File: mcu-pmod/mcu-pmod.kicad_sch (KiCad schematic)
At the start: 51 parts, among them J1 PMOD_DEVICE, J2 XILINX_JTAG, J3 CONN_01X03, J4 CONN_01X03, J5 PMOD_HOST, U1 STM32H735-UFBGA176-25, U2 AT24MAC402

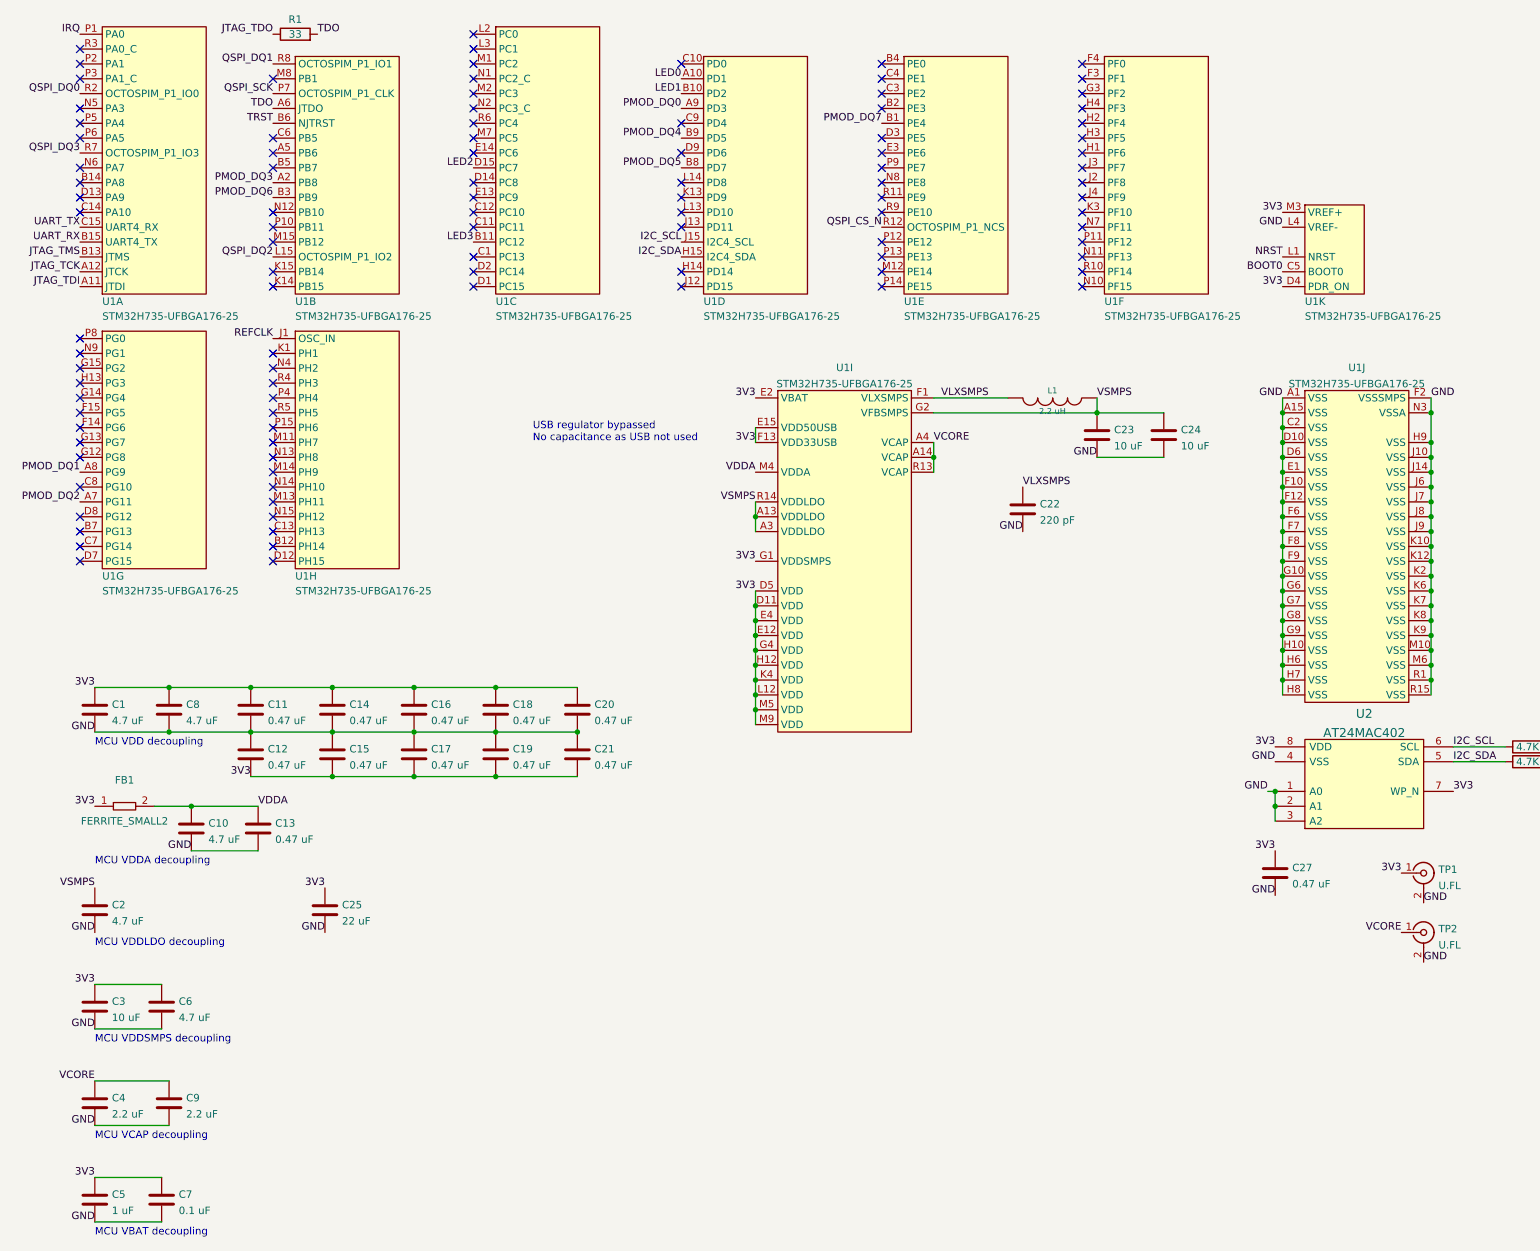
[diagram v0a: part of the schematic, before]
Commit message: v0.2 of mcu-pmod with correct STM32 footprint
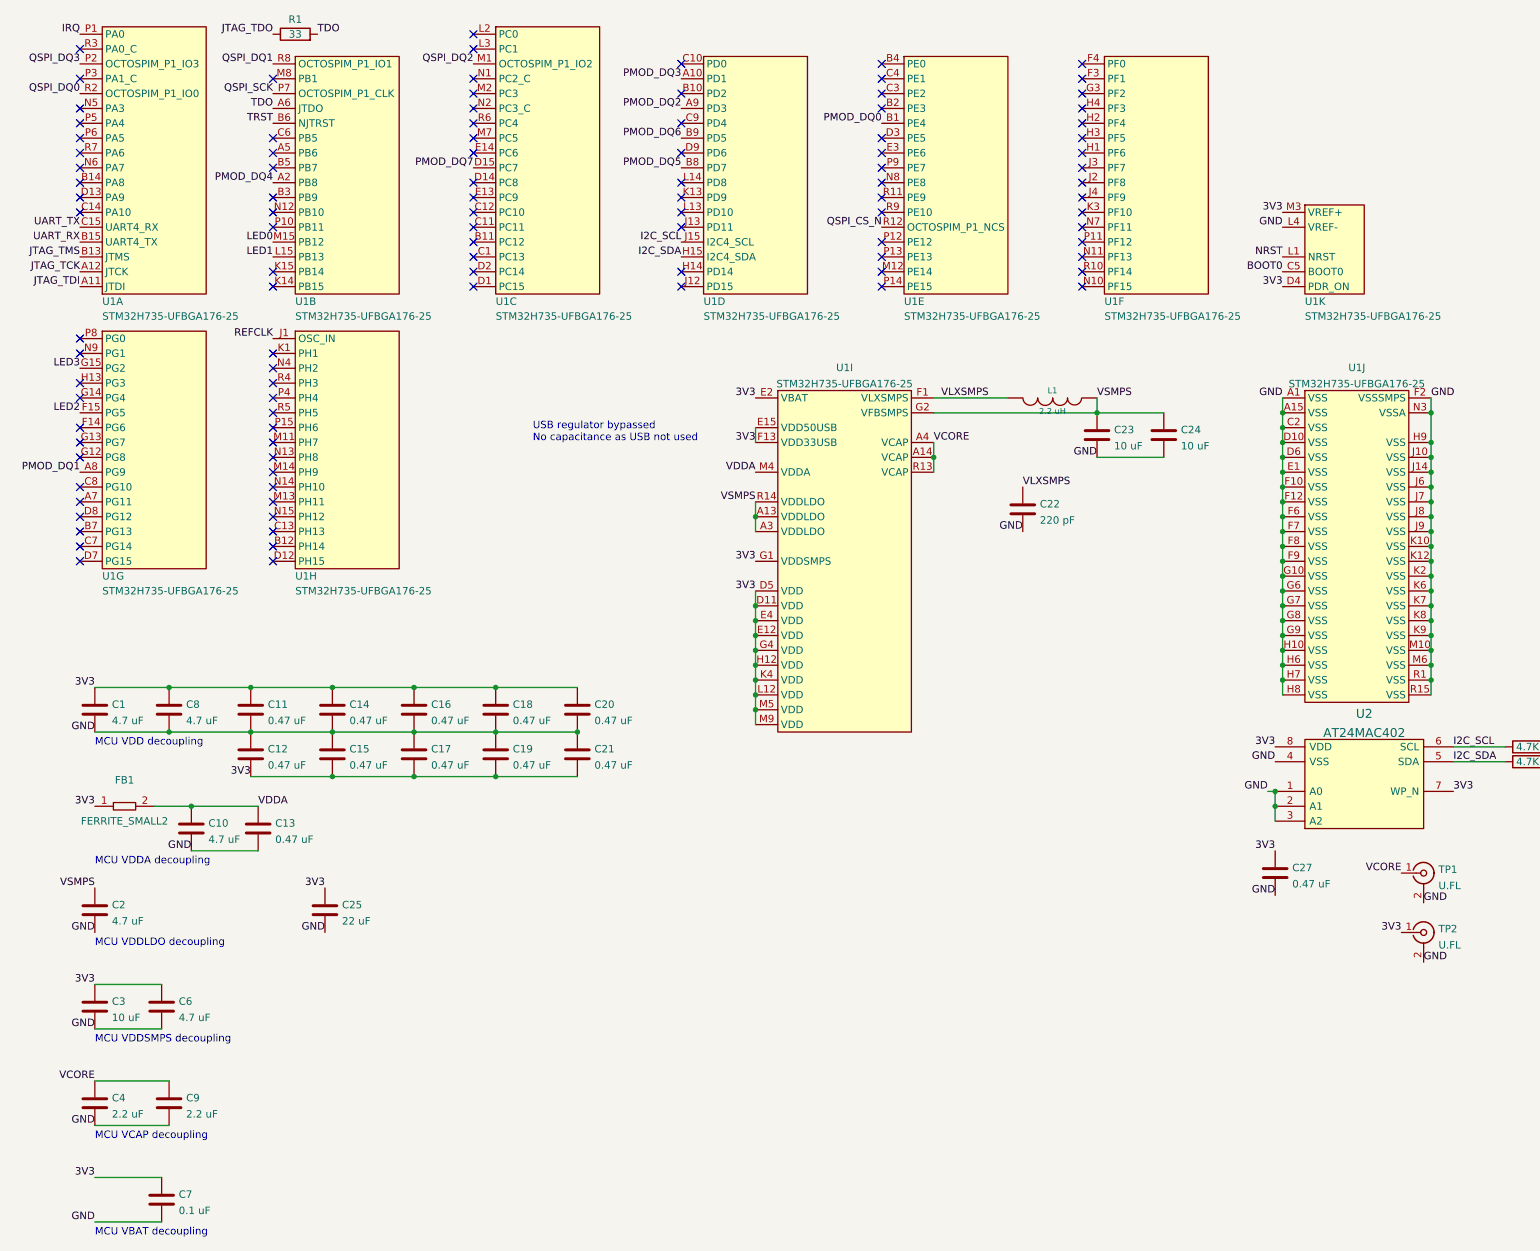
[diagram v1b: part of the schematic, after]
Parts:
- removed C5: 1 uF, azonenberg_pcb:EIA_0603_CAP_NOSILK, symbol device:C
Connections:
- net 3V3: now also TP2.1 (In); no longer TP1.1 (In)
- net LED0: now also U1.M15 (PB12); no longer U1.A10 (PD1)
- net LED1: now also U1.L15 (PB13); no longer U1.B10 (PD2)
- net LED2: now also U1.F15 (PG5); no longer U1.D15 (PC7)
- net LED3: now also U1.G15 (PG2); no longer U1.B11 (PC12)
- net PMOD_DQ0: now also U1.B1 (PE4); no longer U1.A9 (PD3)
- net PMOD_DQ2: now also U1.A9 (PD3); no longer U1.A7 (PG11)
- net PMOD_DQ3: now also U1.A10 (PD1); no longer U1.A2 (PB8)
- net PMOD_DQ4: now also U1.A2 (PB8); no longer U1.B9 (PD5)
- net PMOD_DQ6: now also U1.B9 (PD5); no longer U1.B3 (PB9)
- net PMOD_DQ7: now also U1.D15 (PC7); no longer U1.B1 (PE4)
- net QSPI_DQ2: now also U1.M1 (PC2); no longer U1.L15 (PB13)
- net QSPI_DQ3: now also U1.P2 (PA1); no longer U1.R7 (PA6)
- net VCORE: now also TP1.1 (In); no longer TP2.1 (In)
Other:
- moved on the sheet: U1C
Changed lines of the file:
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@@
   (title_block
     (title "MCU PMOD")
-    (date "2022-05-15")
+    (date "2022-05-31")
     (rev "0.1")
     (company "Antikernel Labs")
@@
   (no_connect (at 57.15 46.99))
   (no_connect (at 57.15 49.53))
-  (no_connect (at 57.15 52.07))
   (no_connect (at 57.15 34.29))
   (no_connect (at 57.15 39.37))
   (no_connect (at 91.44 34.29))
-  (no_connect (at 91.44 21.59))
+  (no_connect (at 127 26.67))
+  (no_connect (at 91.44 52.07))
   (no_connect (at 24.13 29.21))
   (no_connect (at 24.13 31.75))
   (no_connect (at 24.13 34.29))
-  (no_connect (at 24.13 21.59))
   (no_connect (at 24.13 19.05))
   (no_connect (at 24.13 101.6))
@@
   (no_connect (at 24.13 68.58))
   (no_connect (at 24.13 71.12))
-  (no_connect (at 24.13 73.66))
   (no_connect (at 24.13 76.2))
   (no_connect (at 24.13 78.74))
-  (no_connect (at 24.13 81.28))
   (no_connect (at 24.13 83.82))
   (no_connect (at 91.44 16.51))
@@
   (no_connect (at 24.13 44.45))
   (no_connect (at 24.13 41.91))
+  (no_connect (at 24.13 36.83))
+  (no_connect (at 24.13 96.52))
+  (no_connect (at 57.15 44.45))
   (no_connect (at 91.44 29.21))
   (no_connect (at 91.44 26.67))
@@
     (effects (font (size 1.27 1.27)) (justify right bottom))
   )
-  (label "VCORE" (at 250.19 170.18 180)
+  (label "VCORE" (at 250.19 160.02 180)
     (effects (font (size 1.27 1.27)) (justify right bottom))
   )
@@
     (effects (font (size 1.27 1.27)) (justify right bottom))
   )
-  (label "LED0" (at 127 24.13 180)
+  (label "LED0" (at 57.15 52.07 180)
     (effects (font (size 1.27 1.27)) (justify right bottom))
   )
@@
     (effects (font (size 1.27 1.27)) (justify right bottom))
   )
-  (label "PMOD_DQ4" (at 127 34.29 180)
+  (label "PMOD_DQ4" (at 57.15 41.91 180)
     (effects (font (size 1.27 1.27)) (justify right bottom))
   )
@@
     (effects (font (size 1.27 1.27)) (justify right bottom))
   )
-  (label "QSPI_DQ2" (at 57.15 54.61 180)
+  (label "QSPI_DQ2" (at 91.44 21.59 180)
     (effects (font (size 1.27 1.27)) (justify right bottom))
   )
@@
     (effects (font (size 1.27 1.27)) (justify left bottom))
   )
-  (label "3V3" (at 250.19 160.02 180)
+  (label "3V3" (at 250.19 170.18 180)
     (effects (font (size 1.27 1.27)) (justify right bottom))
   )
@@
     (effects (font (size 1.27 1.27)) (justify right bottom))
   )
-  (label "LED2" (at 91.44 39.37 180)
+  (label "LED2" (at 24.13 81.28 180)
     (effects (font (size 1.27 1.27)) (justify right bottom))
   )
@@
     (effects (font (size 1.27 1.27)) (justify right bottom))
   )
-  (label "PMOD_DQ6" (at 57.15 44.45 180)
+  (label "PMOD_DQ6" (at 127 34.29 180)
     (effects (font (size 1.27 1.27)) (justify right bottom))
   )
@@
     (effects (font (size 1.27 1.27)) (justify right bottom))
   )
-  (label "PMOD_DQ7" (at 161.29 31.75 180)
+  (label "PMOD_DQ7" (at 91.44 39.37 180)
     (effects (font (size 1.27 1.27)) (justify right bottom))
   )
@@
     (effects (font (size 1.27 1.27)) (justify right bottom))
   )
-  (label "PMOD_DQ2" (at 24.13 96.52 180)
+  (label "PMOD_DQ2" (at 127 29.21 180)
     (effects (font (size 1.27 1.27)) (justify right bottom))
   )
@@
     (effects (font (size 1.27 1.27)) (justify right bottom))
   )
-  (label "PMOD_DQ0" (at 127 29.21 180)
+  (label "PMOD_DQ0" (at 161.29 31.75 180)
     (effects (font (size 1.27 1.27)) (justify right bottom))
   )
@@
     (effects (font (size 1.27 1.27)) (justify right bottom))
   )
-  (label "LED1" (at 127 26.67 180)
+  (label "LED1" (at 57.15 54.61 180)
     (effects (font (size 1.27 1.27)) (justify right bottom))
   )
@@
     (effects (font (size 1.27 1.27)) (justify left bottom))
   )
-  (label "PMOD_DQ3" (at 57.15 41.91 180)
+  (label "PMOD_DQ3" (at 127 24.13 180)
     (effects (font (size 1.27 1.27)) (justify right bottom))
   )
@@
     (effects (font (size 1.27 1.27)) (justify right bottom))
   )
-  (label "QSPI_DQ3" (at 24.13 36.83 180)
+  (label "QSPI_DQ3" (at 24.13 21.59 180)
     (effects (font (size 1.27 1.27)) (justify right bottom))
   )
@@
     (effects (font (size 1.27 1.27)) (justify right bottom))
   )
-  (label "LED3" (at 91.44 52.07 180)
+  (label "LED3" (at 24.13 73.66 180)
     (effects (font (size 1.27 1.27)) (justify right bottom))
   )
@@
     (pin "N6")
     (pin "P1")
-    (pin "P2")
+    (pin "P2" (alternate "OCTOSPIM_P1_IO3"))
     (pin "P3")
     (pin "P5")
@@
     (pin "R2" (alternate "OCTOSPIM_P1_IO0"))
     (pin "R3")
-    (pin "R7" (alternate "OCTOSPIM_P1_IO3"))
+    (pin "R7")
   )
   (symbol (lib_id "device:LED") (at 306.07 114.3 0) (unit 1)
@@
     (pin "K14")
     (pin "K15")
-    (pin "L15" (alternate "OCTOSPIM_P1_IO2"))
+    (pin "L15")
     (pin "M15")
     (pin "M8")
@@
     )
     (property "Datasheet" "" (id 3) (at 81.28 132.08 0)
-      (effects (font (size 1.27 1.27)) hide)
-    )
-    (pin "1")
-    (pin "2")
-  )
-  (symbol (lib_id "device:C") (at 26.67 215.9 0) (unit 1)
-    (in_bom yes) (on_board yes) (fields_autoplaced)
-    (property "Reference" "C5" (id 0) (at 29.591 214.9915 0)
-      (effects (font (size 1.27 1.27)) (justify left))
-    )
-    (property "Value" "1 uF" (id 1) (at 29.591 217.7666 0)
-      (effects (font (size 1.27 1.27)) (justify left))
-    )
-    (property "Footprint" "azonenberg_pcb:EIA_0603_CAP_NOSILK" (id 2) (at 27.6352 219.71 0)
-      (effects (font (size 1.27 1.27)) hide)
-    )
-    (property "Datasheet" "" (id 3) (at 26.67 215.9 0)
       (effects (font (size 1.27 1.27)) hide)
     )
@@
     (pin "L2")
     (pin "L3")
-    (pin "M1")
+    (pin "M1" (alternate "OCTOSPIM_P1_IO2"))
     (pin "M2")
     (pin "M7")
@@
       (reference "C4") (unit 1) (value "2.2 uF") (footprint "azonenberg_pcb:EIA_0603_CAP_NOSILK")
     )
-    (path "/627848a1-c2ff-49d3-a948-d18bdc2147ed"
-      (reference "C5") (unit 1) (value "1 uF") (footprint "azonenberg_pcb:EIA_0603_CAP_NOSILK")
-    )
     (path "/9b9f470f-0183-4044-ae5b-bbe815ad4f09"

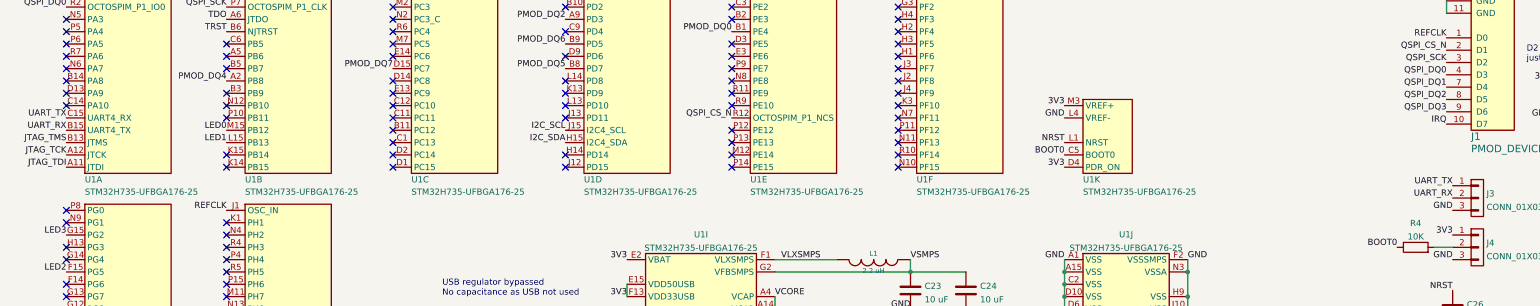
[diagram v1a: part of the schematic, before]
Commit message: Fixed TX/RX swap in schematic
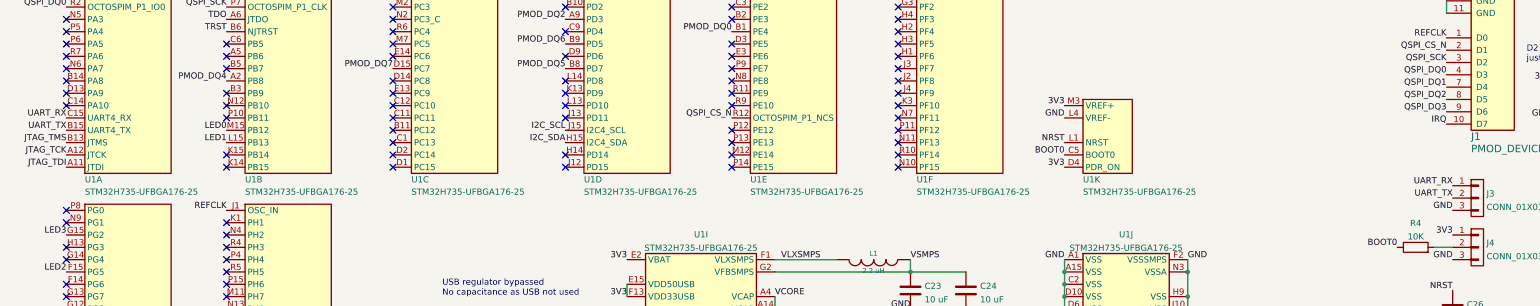
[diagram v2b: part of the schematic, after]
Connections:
- net UART_RX: now also J3.1 (P1), U1.C15 (PA11); no longer J3.2 (P2), U1.B15 (PA12)
- net UART_TX: now also J3.2 (P2), U1.B15 (PA12); no longer J3.1 (P1), U1.C15 (PA11)
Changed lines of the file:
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@@
     (effects (font (size 1.27 1.27)) (justify left bottom))
   )
-  (label "UART_TX" (at 309.88 63.5 180)
+  (label "UART_TX" (at 309.88 66.04 180)
     (effects (font (size 1.27 1.27)) (justify right bottom))
   )
@@
     (effects (font (size 1.27 1.27)) (justify right bottom))
   )
-  (label "UART_RX" (at 309.88 66.04 180)
+  (label "UART_RX" (at 309.88 63.5 180)
     (effects (font (size 1.27 1.27)) (justify right bottom))
   )
@@
     (effects (font (size 1.27 1.27)) (justify right bottom))
   )
-  (label "UART_RX" (at 24.13 52.07 180)
+  (label "UART_RX" (at 24.13 49.53 180)
     (effects (font (size 1.27 1.27)) (justify right bottom))
   )
@@
     (effects (font (size 1.27 1.27)) (justify right bottom))
   )
-  (label "UART_TX" (at 24.13 49.53 180)
-    (effects (font (size 1.27 1.27)) (justify right bottom))
-  )
+  (label "UART_TX" (at 24.13 52.07 180)
+    (effects (font (size 1.27 1.27)) (justify right bottom))
+  )
